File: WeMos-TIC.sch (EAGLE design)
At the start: 21 parts, among them Q2 BSS138

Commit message: Bump to V1.1
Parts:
- removed D5: 1N4148, Seeed-Discrete:D-ESD-2P-CESD5V0D1
- removed JP2: JUMPER-PAD-2-NC_BY_TRACE, SparkFun-Passives:JUMPER-PAD-2-NC_BY_TRACE
- removed L1: WS2812B, _c2h:WS2812B5MM
- removed L2: WS2812B, _c2h:WS2812BLONG
- removed U$1: PAD, _c2h:PAD-JUMPER-SWAPSWAP
- added D1: 1N4148, microbuilder:DIODESOD-523
- added LED: WS2812-2020, SparkFun-LED:WS2812-2020
- added R6: 1K, _c2h:RESISTOR0603-RES
- added RX: TIC-RX, SparkFun-Jumpers:JUMPER-SMT_3_1-NC_TRACE_SILK
- added TIC: LED0603, _c2h:LED0603
- C1: device _c2h:CAP0805-CAP -> _c2h:CAP0402-CAP-OK
- R1, R2, R5: device _c2h:RESISTOR0805-RES -> _c2h:RESISTOR0603-RES
- R3: value 1.2K -> 220; device _c2h:RESISTOR0805-RES -> _c2h:RESISTOR0603-RES
- R4: value 10k -> 3K3; device _c2h:RESISTOR0805-RES -> _c2h:RESISTOR0603-RES
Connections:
- net MISO renamed GPIO12
- removed net MOSI: JP3.6, JP7.6
- removed net N$6: L1.DOUT, L2.DOUT
- removed net SCK: JP3.4, JP7.4, L1.DIN, L2.DIN
- removed net V+O: I2C_OLED1.1, U$1.3
- removed net V-O: I2C_OLED1.2, U$1.2
- new net GPIO13: JP3.6, JP7.6, RX.3
- new net GPIO14: JP3.4, JP7.4, LED.DI
- new net N$1: R6.2, TIC.MINUS
- new net TIC-RX: Q2.D, R5.1, R6.1, RX.2
- net 3V3: now also I2C_OLED1.2, JP5.2, TIC.PLUS; no longer U$1.4
- net 5V: now also D1.A, JP5.1; no longer D5.1, JP2.2
- net GND: now also I2C_OLED1.1, LED.VSS; no longer JP5.1, JP5.2, L1.GND, L2.GND, U$1.1
- net GPIO3: now also RX.1; no longer Q2.D, R5.1
- net VLED: now also D1.C, LED.VDD; no longer D5.2, JP2.1, L1.VDD, L2.VDD
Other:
- note added: "MISO"
- note added: "MOSI"
- note added: "SCK"
- note removed: "GPIO12"
- note removed: "GPIO13"
- note removed: "GPIO14"
- moved on the sheet: C1, JP5, JP7, JP8, R5

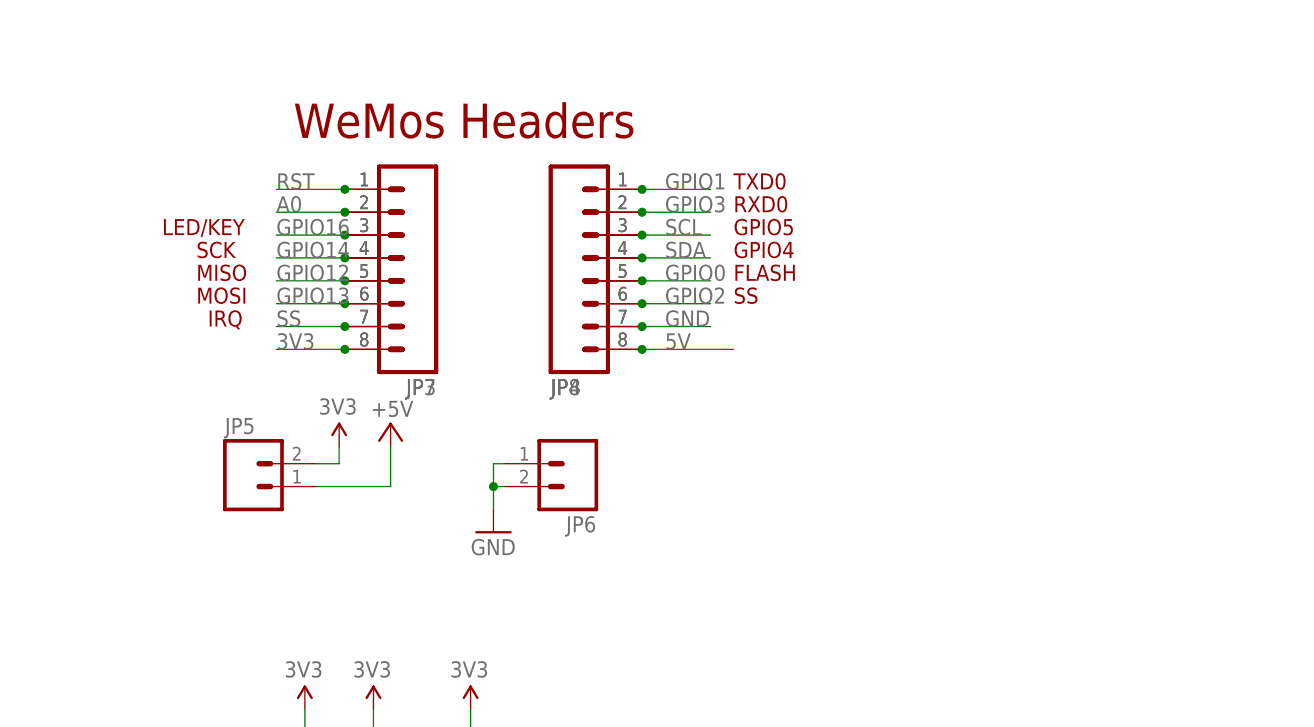
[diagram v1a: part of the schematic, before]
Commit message: Added detailed pinout
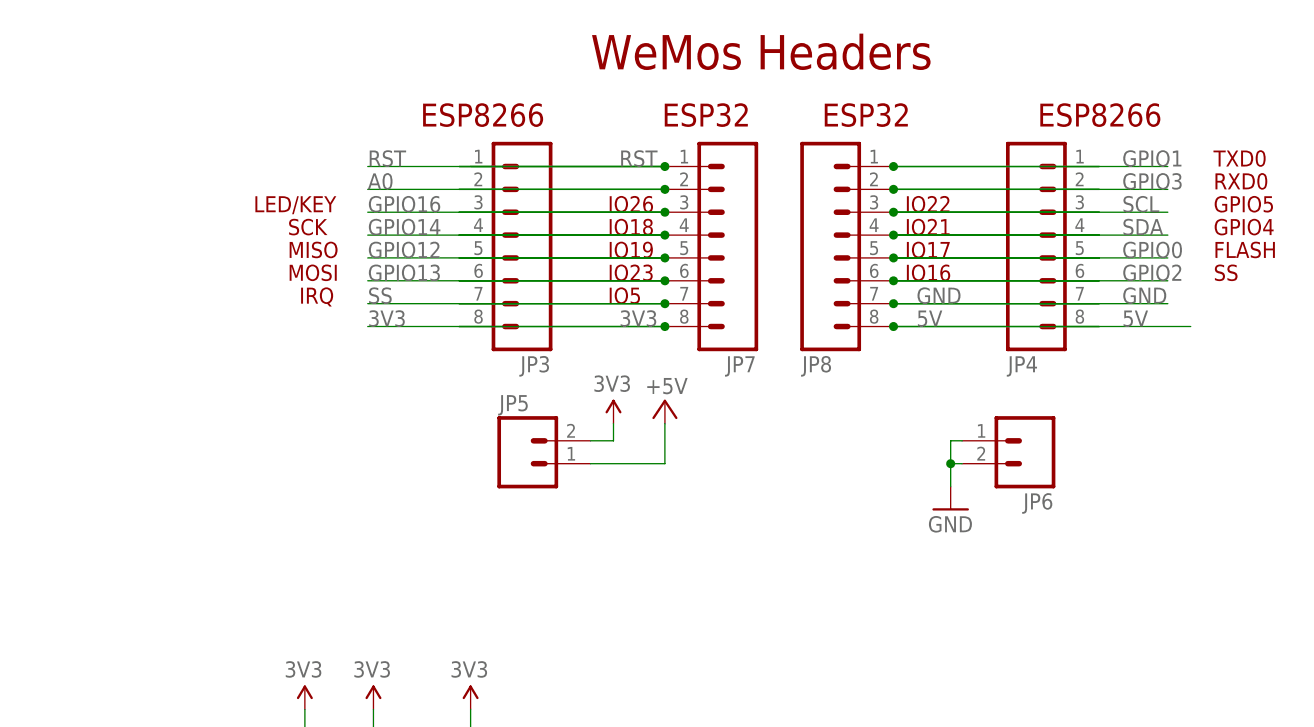
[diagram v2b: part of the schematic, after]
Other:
- note added: "ESP32"
- note added: "ESP8266"
- note added: "IO16"
- note added: "IO17"
- note added: "IO18"
- note added: "IO19"
- note added: "IO21"
- note added: "IO22"
- note added: "IO23"
- note added: "IO26"
- note added: "IO5"
- moved on the sheet: JP3, JP4, JP5, JP6, JP7, JP8

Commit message: Bump to v1.2
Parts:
- removed JP7, JP8: (no value), SparkFun-Connectors:M08NO_SILK_FEMALE_PTH
- removed Q2: BSS138, Seeed-Discrete:MOSFET-N-''
- removed TINFO: 1X2-3.5MM, adafruit:1X2-3.5MM
- added J1: KF2EDGR-3.81-2P, _c2h:1X2-3.5MM-3.5MM
- added J2: Qwiic Connector, _c2h:QWIIC_CONNECTOR
- added JLED: JUMPER-PAD-2-NC_BY_TRACE, SparkFun-Passives:JUMPER-PAD-2-NC_BY_TRACE
- added Q1: BSS138, _c2h:SMD-MOSFET-N-CH-20V-2.1A-CJ2302(SOT-23)
- R1, R2, R4, R5, R6: device _c2h:RESISTOR0603-RES -> _c2h:RESISTOR0402-RES
- R3: value 220 -> 2K; device _c2h:RESISTOR0603-RES -> adafruit:TRIMPOTTC33X
- TIC: value LED0603 -> BLUE; device _c2h:LED0603 -> OPL_Optoelectronics:SMD-LED-CLEAR-BLUE(0402)
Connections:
- new net LTIC: JLED.2, TIC.+
- net 3V3: now also J2.2, JLED.1; no longer JP7.8, TIC.PLUS
- net 5V: no longer JP8.8
- net A0: no longer JP7.2
- net GND: now also J2.1, Q1.S; no longer JP8.7, Q2.S
- net GPIO0: no longer JP8.5
- net GPIO1: no longer JP8.1
- net GPIO12: no longer JP7.5
- net GPIO13: no longer JP7.6
- net GPIO14: no longer JP7.4
- net GPIO16: no longer JP7.3
- net GPIO2: no longer JP8.6
- net GPIO3: no longer JP8.2
- net N$1: now also TIC.-; no longer TIC.MINUS
- net N$2: now also Q1.G; no longer Q2.G
- net N$3: now also R3.A; no longer R3.1
- net N$4: now also J1.1; no longer TINFO.1
- net N$5: now also J1.2, R3.S; no longer R3.2, TINFO.2
- net RST: no longer JP7.1
- net SCL: now also J2.4; no longer JP8.3
- net SDA: now also J2.3; no longer JP8.4
- net SS: no longer JP7.7
- net TIC-RX: now also Q1.D; no longer Q2.D
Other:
- note added: "Téléinfo"
- moved on the sheet: R5, R6
